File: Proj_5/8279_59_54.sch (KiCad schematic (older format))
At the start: 44 parts, among them J4 Conn_02x07_Counter_Clockwise, J5 Conn_02x07_Counter_Clockwise, SW10 Switch_SW_SPST, SW11 Switch_SW_SPST, SW12 Switch_SW_SPST, SW13 Switch_SW_SPST, SW14 Switch_SW_SPST, SW15 Switch_SW_SPST, SW16 Switch_SW_SPST, SW17 Switch_SW_SPST, SW18 Switch_SW_SPST, SW19 Switch_SW_SPST, SW2 Shift, SW20 Switch_SW_SPST, SW21 Switch_SW_SPST, SW22 Switch_SW_SPST, SW23 Switch_SW_SPST, SW24 NMI Button, SW25 Reset Button, SW26 IR0 Button, SW3 Switch_SW_SPST, SW4 Switch_SW_SPST, SW5 Switch_SW_SPST, SW6 Switch_SW_SPST, SW7 CTRL, SW8 Switch_SW_SPST, SW9 Switch_SW_SPST, U10 8259, U11 8254, U17 pkd8279, U18 74LS138, U48 MAX6816, U49 MAX6816, U50 MAX6816

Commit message: Destroyed errors
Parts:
- removed U?: 74LVC1G11, symbol 74xGxx:74LVC1G11
- removed U?: 74LVC1G08, symbol 74xGxx:74LVC1G08
- added U35, U58: 74AHC1G02, symbol 74xGxx:74AHC1G02
- added U38: 74LVC1G08, symbol 74xGxx:74LVC1G08
- gave numbers to parts that had none: 1
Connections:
- net A16: now also U35.2
- net A17: now also U35.1
- net A18: now also U58.2
- net A19: now also U58.1
- net GND: now also U35.3 (GND), U38.3 (GND), U58.3 (GND)
- net VCC: now also U35.5 (VCC), U38.5 (VCC), U58.5 (VCC)
- net at U60.1 (I1): now also U38.4
- new net: U38.1, U58.4
- new net: U35.4, U38.2
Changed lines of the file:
@@
 	7200 2700 7350 2700
 $Comp
-L Logic_Programmable:PAL16L8 U?
+L Logic_Programmable:PAL16L8 U60
 U 1 1 5ED93710
 P 2300 2350
-F 0 "U?" H 2300 3231 50  0000 C CNN
+F 0 "U60" H 2300 3231 50  0000 C CNN
 F 1 "PAL16L8" H 2300 3140 50  0000 C CNN
 F 2 "" H 2300 2350 50  0001 C CNN
@@
 Text HLabel 1800 2750 0    50   Input ~ 0
 A9
-$Comp
-L 74xGxx:74LVC1G11 U?
-U 1 1 5EE4156C
-P 1300 1850
-F 0 "U?" H 1300 2164 50  0000 C CNN
-F 1 "74LVC1G11" H 1300 2073 50  0000 C CNN
-F 2 "" H 1300 1850 50  0001 C CNN
-F 3 "http://www.ti.com/lit/sg/scyt129e/scyt129e.pdf" H 1300 1850 50  0001 C CNN
-	1    1300 1850
-	1    0    0    -1
-$EndComp
-$Comp
-L 74xGxx:74LVC1G08 U?
-U 1 1 5EE43827
-P 1000 2200
-F 0 "U?" V 1021 2070 50  0000 R CNN
-F 1 "74LVC1G08" V 930 2070 50  0000 R CNN
-F 2 "" H 1000 2200 50  0001 C CNN
-F 3 "http://www.ti.com/lit/sg/scyt129e/scyt129e.pdf" H 1000 2200 50  0001 C CNN
-	1    1000 2200
-	0    -1   -1   0
-$EndComp
-Text HLabel 950  2500 3    50   Input ~ 0
-A19
-Text HLabel 1050 2500 3    50   Input ~ 0
-A18
-Text HLabel 1000 1850 0    50   Input ~ 0
-A17
-Text HLabel 1000 1750 0    50   Input ~ 0
-A16
-Wire Wire Line
-	1600 1850 1800 1850
 Text HLabel 2800 2150 2    50   Input ~ 0
 A4
@@
 	5550 800  6450 800
 $Comp
-L power:GND #PWR?
+L power:GND #PWR082
 U 1 1 5EF0D1C7
 P 2300 2950
-F 0 "#PWR?" H 2300 2700 50  0001 C CNN
+F 0 "#PWR082" H 2300 2700 50  0001 C CNN
 F 1 "GND" H 2305 2777 50  0000 C CNN
 F 2 "" H 2300 2950 50  0001 C CNN
@@
 $EndComp
 $Comp
-L power:GND #PWR?
+L power:GND #PWR097
 U 1 1 5EF1007D
 P 5550 5650
-F 0 "#PWR?" H 5550 5400 50  0001 C CNN
+F 0 "#PWR097" H 5550 5400 50  0001 C CNN
 F 1 "GND" H 5555 5477 50  0000 C CNN
 F 2 "" H 5550 5650 50  0001 C CNN
@@
 	1    0    0    -1
 $EndComp
+$Comp
+L 74xGxx:74AHC1G02 U58
+U 1 1 5F4DAB3E
+P 1450 1000
+F 0 "U58" V 1379 1130 50  0000 L CNN
+F 1 "74AHC1G02" V 1470 1130 50  0000 L CNN
+F 2 "" H 1450 1000 50  0001 C CNN
+F 3 "http://www.ti.com/lit/sg/scyt129e/scyt129e.pdf" H 1450 1000 50  0001 C CNN
+	1    1450 1000
+	0    1    1    0
+$EndComp
+$Comp
+L 74xGxx:74AHC1G02 U35
+U 1 1 5F4DE98E
+P 1100 1250
+F 0 "U35" H 1075 1517 50  0000 C CNN
+F 1 "74AHC1G02" H 1075 1426 50  0000 C CNN
+F 2 "" H 1100 1250 50  0001 C CNN
+F 3 "http://www.ti.com/lit/sg/scyt129e/scyt129e.pdf" H 1100 1250 50  0001 C CNN
+	1    1100 1250
+	1    0    0    -1
+$EndComp
+$Comp
+L 74xGxx:74LVC1G08 U38
+U 1 1 5F4E0E05
+P 1400 1550
+F 0 "U38" V 1329 1680 50  0000 L CNN
+F 1 "74LVC1G08" V 1420 1680 50  0000 L CNN
+F 2 "" H 1400 1550 50  0001 C CNN
+F 3 "http://www.ti.com/lit/sg/scyt129e/scyt129e.pdf" H 1400 1550 50  0001 C CNN
+	1    1400 1550
+	0    1    1    0
+$EndComp
+Wire Wire Line
+	1400 1850 1400 1800
+Wire Wire Line
+	1400 1850 1800 1850
+Text HLabel 1500 700  1    50   Input ~ 0
+A19
+Text HLabel 1400 700  1    50   Input ~ 0
+A18
+Text HLabel 800  1200 0    50   Input ~ 0
+A17
+Text HLabel 800  1300 0    50   Input ~ 0
+A16
 $EndSCHEMATC

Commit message: 11 errors left
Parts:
- removed U35, U58: 74AHC1G02, symbol 74xGxx:74AHC1G02
- removed U38: 74LVC1G08, symbol 74xGxx:74LVC1G08
- removed U60: PAL16L8, symbol Logic_Programmable:PAL16L8
- added U35, U38: PAL16L8, symbol Logic_Programmable:PAL16L8
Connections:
- net A0: now also U38.8 (I8)
- net A1: now also U38.7 (I7); no longer U10.27 (A0), U17.21 (A0)
- net A10: now also U35.11 (I10)
- net A11: now also U35.9 (I9)
- net A12: now also U35.8 (I8)
- net A13: now also U35.7 (I7)
- net A14: now also U35.6 (I6)
- net A15: now also U35.5 (I5)
- net A16: now also U35.4 (I4)
- net A17: now also U35.3 (I3)
- net A18: now also U35.2 (I2)
- net A19: now also U35.1 (I1)
- net A2: now also U38.6 (I6)
- net A3: now also U38.5 (I5)
- net A4: now also U38.4 (I4)
- net A5: now also U38.3 (I3)
- net A6: now also U38.2 (I2)
- net A7: now also U38.1 (I1)
- net A8: now also U35.17 (I03)
- net A9: now also U35.18 (IO2)
- net GND: now also C19.2, U35.10 (GND), U38.10 (GND)
- net VCC: now also U35.20 (VCC), U38.20 (VCC)
- net at U17.22 (~CS): now also U38.17 (I03); no longer U10.1 (~CS~)
- net at U11.19 (A0): now also U38.14 (IO6)
- net at U11.20 (A1): now also U38.13 (IO7)
- net at U11.21 (~CS~): now also U38.15 (IO5)
- net INT: now reaches U10.17 (INT)
- net ~INTA: now reaches U10.26 (~INTA~)
- new net: U17.21 (A0), U38.16 (IO4)
- new net: U10.1 (~CS~), U38.19 (IO1)
- new net: U10.27 (A0), U38.18 (IO2)
- new net: U35.19 (IO1), U38.11 (I10)
- no-connect marks 22 -> 28
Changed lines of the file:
@@
 L power:VCC #PWR062
 U 1 1 5EA94B2B
-P 5100 3150
-F 0 "#PWR062" H 5100 3000 50  0001 C CNN
-F 1 "VCC" H 5118 3323 50  0000 C CNN
-F 2 "" H 5100 3150 50  0001 C CNN
-F 3 "" H 5100 3150 50  0001 C CNN
-	1    5100 3150
+P 6000 3150
+F 0 "#PWR062" H 6000 3000 50  0001 C CNN
+F 1 "VCC" H 6018 3323 50  0000 C CNN
+F 2 "" H 6000 3150 50  0001 C CNN
+F 3 "" H 6000 3150 50  0001 C CNN
+	1    6000 3150
 	0    -1   -1   0
 $EndComp
@@
 Wire Wire Line
 	7200 2850 7200 2700
-Connection ~ 6200 3150
 Wire Wire Line
 	6950 3150 7100 3150
@@
 	5600 6150 6550 6150
 Wire Wire Line
-	5100 3150 6200 3150
-Wire Wire Line
 	5500 800  5550 800
 Wire Wire Line
@@
 Wire Wire Line
 	7200 2700 7350 2700
-$Comp
-L Logic_Programmable:PAL16L8 U60
-U 1 1 5ED93710
-P 2300 2350
-F 0 "U60" H 2300 3231 50  0000 C CNN
-F 1 "PAL16L8" H 2300 3140 50  0000 C CNN
-F 2 "" H 2300 2350 50  0001 C CNN
-F 3 "" H 2300 2350 50  0001 C CNN
-	1    2300 2350
-	1    0    0    -1
-$EndComp
-Text HLabel 1800 1950 0    50   Input ~ 0
-A15
-Text HLabel 1800 2050 0    50   Input ~ 0
-A14
-Text HLabel 1800 2150 0    50   Input ~ 0
-A13
-Text HLabel 1800 2250 0    50   Input ~ 0
-A12
-Text HLabel 1800 2350 0    50   Input ~ 0
-A11
-Text HLabel 1800 2450 0    50   Input ~ 0
-A10
-Text HLabel 2800 1950 2    50   Input ~ 0
-A6
-Text HLabel 2800 2050 2    50   Input ~ 0
-A5
-Text HLabel 1800 2550 0    50   Input ~ 0
-A7
-Text HLabel 1800 2650 0    50   Input ~ 0
-A8
-Text HLabel 1800 2750 0    50   Input ~ 0
-A9
-Text HLabel 2800 2150 2    50   Input ~ 0
-A4
-Text HLabel 2800 2250 2    50   Input ~ 0
-A3
-Text HLabel 2800 2350 2    50   Input ~ 0
-A2
-Text HLabel 2800 2450 2    50   Input ~ 0
-A0
-Wire Wire Line
-	2800 2550 5200 2550
-Wire Wire Line
-	5200 2550 5200 2300
 Wire Wire Line
 	5200 2300 5850 2300
 Wire Wire Line
-	5200 2550 5200 4850
-Wire Wire Line
-	5200 4850 5550 4850
-Connection ~ 5200 2550
-Text HLabel 5550 5150 0    50   Input ~ 0
-A1
-Text HLabel 5850 2100 0    50   Input ~ 0
-A1
-NoConn ~ 2800 1850
-Wire Wire Line
-	5550 800  5550 1650
-Wire Wire Line
-	5550 1650 2300 1650
+	5550 800  5550 1450
 Connection ~ 5550 800
 Wire Wire Line
 	5550 800  6450 800
-$Comp
-L power:GND #PWR082
-U 1 1 5EF0D1C7
-P 2300 2950
-F 0 "#PWR082" H 2300 2700 50  0001 C CNN
-F 1 "GND" H 2305 2777 50  0000 C CNN
-F 2 "" H 2300 2950 50  0001 C CNN
-F 3 "" H 2300 2950 50  0001 C CNN
-	1    2300 2950
-	1    0    0    -1
-$EndComp
 $Comp
 L power:GND #PWR097
@@
 $EndComp
 $Comp
-L 74xGxx:74AHC1G02 U58
-U 1 1 5F4DAB3E
-P 1450 1000
-F 0 "U58" V 1379 1130 50  0000 L CNN
-F 1 "74AHC1G02" V 1470 1130 50  0000 L CNN
-F 2 "" H 1450 1000 50  0001 C CNN
-F 3 "http://www.ti.com/lit/sg/scyt129e/scyt129e.pdf" H 1450 1000 50  0001 C CNN
-	1    1450 1000
-	0    1    1    0
-$EndComp
-$Comp
-L 74xGxx:74AHC1G02 U35
-U 1 1 5F4DE98E
-P 1100 1250
-F 0 "U35" H 1075 1517 50  0000 C CNN
-F 1 "74AHC1G02" H 1075 1426 50  0000 C CNN
-F 2 "" H 1100 1250 50  0001 C CNN
-F 3 "http://www.ti.com/lit/sg/scyt129e/scyt129e.pdf" H 1100 1250 50  0001 C CNN
-	1    1100 1250
-	1    0    0    -1
-$EndComp
-$Comp
-L 74xGxx:74LVC1G08 U38
-U 1 1 5F4E0E05
-P 1400 1550
-F 0 "U38" V 1329 1680 50  0000 L CNN
-F 1 "74LVC1G08" V 1420 1680 50  0000 L CNN
-F 2 "" H 1400 1550 50  0001 C CNN
-F 3 "http://www.ti.com/lit/sg/scyt129e/scyt129e.pdf" H 1400 1550 50  0001 C CNN
-	1    1400 1550
-	0    1    1    0
-$EndComp
-Wire Wire Line
-	1400 1850 1400 1800
-Wire Wire Line
-	1400 1850 1800 1850
-Text HLabel 1500 700  1    50   Input ~ 0
+L Logic_Programmable:PAL16L8 U35
+U 1 1 5EC20107
+P 1350 4050
+F 0 "U35" H 1350 4931 50  0000 C CNN
+F 1 "PAL16L8" H 1350 4840 50  0000 C CNN
+F 2 "" H 1350 4050 50  0001 C CNN
+F 3 "" H 1350 4050 50  0001 C CNN
+	1    1350 4050
+	1    0    0    -1
+$EndComp
+Text HLabel 850  3550 0    50   Input ~ 0
 A19
-Text HLabel 1400 700  1    50   Input ~ 0
+Text HLabel 850  3650 0    50   Input ~ 0
 A18
-Text HLabel 800  1200 0    50   Input ~ 0
+Text HLabel 850  3750 0    50   Input ~ 0
 A17
-Text HLabel 800  1300 0    50   Input ~ 0
+Text HLabel 850  3850 0    50   Input ~ 0
 A16
+Text HLabel 850  3950 0    50   Input ~ 0
+A15
+Text HLabel 850  4050 0    50   Input ~ 0
+A14
+Text HLabel 850  4150 0    50   Input ~ 0
+A13
+Text HLabel 850  4250 0    50   Input ~ 0
+A12
+Text HLabel 850  4350 0    50   Input ~ 0
+A11
+Text HLabel 850  4450 0    50   Input ~ 0
+A10
+Text HLabel 1850 3650 2    50   Input ~ 0
+A9
+Text HLabel 1850 3750 2    50   Input ~ 0
+A8
+$Comp
+L Logic_Programmable:PAL16L8 U38
+U 1 1 5ECCAFFC
+P 1400 2150
+F 0 "U38" H 1400 3031 50  0000 C CNN
+F 1 "PAL16L8" H 1400 2940 50  0000 C CNN
+F 2 "" H 1400 2150 50  0001 C CNN
+F 3 "" H 1400 2150 50  0001 C CNN
+	1    1400 2150
+	1    0    0    -1
+$EndComp
+Wire Wire Line
+	1850 3550 1850 3000
+Wire Wire Line
+	1850 3000 900  3000
+Wire Wire Line
+	900  3000 900  2550
+Text HLabel 900  1650 0    50   Input ~ 0
+A7
+Text HLabel 900  1750 0    50   Input ~ 0
+A6
+Text HLabel 900  1850 0    50   Input ~ 0
+A5
+Text HLabel 900  1950 0    50   Input ~ 0
+A4
+Text HLabel 900  2050 0    50   Input ~ 0
+A3
+Text HLabel 900  2150 0    50   Input ~ 0
+A2
+Text HLabel 900  2250 0    50   Input ~ 0
+A1
+Text HLabel 900  2350 0    50   Input ~ 0
+A0
+Wire Wire Line
+	1400 1450 2100 1450
+Wire Wire Line
+	1900 1650 5200 1650
+Wire Wire Line
+	5200 1650 5200 2300
+Connection ~ 6200 3150
+Wire Wire Line
+	1900 1850 5000 1850
+Wire Wire Line
+	5000 1850 5000 4850
+Wire Wire Line
+	5000 4850 5550 4850
+Wire Wire Line
+	1900 1750 5100 1750
+Wire Wire Line
+	5100 1750 5100 2100
+Wire Wire Line
+	5100 2100 5850 2100
+Wire Wire Line
+	5550 5150 4900 5150
+Wire Wire Line
+	4900 5150 4900 1950
+Wire Wire Line
+	1900 1950 4900 1950
+Wire Wire Line
+	1900 2050 4600 2050
+Wire Wire Line
+	4600 2050 4600 8200
+Wire Wire Line
+	4600 8200 5950 8200
+Wire Wire Line
+	1900 2150 4400 2150
+Wire Wire Line
+	4400 2150 4400 7900
+Wire Wire Line
+	4400 7900 5950 7900
+Wire Wire Line
+	1900 2250 4200 2250
+Wire Wire Line
+	4200 2250 4200 8000
+Wire Wire Line
+	4200 8000 5950 8000
+NoConn ~ 1900 2350
+NoConn ~ 900  2450
+NoConn ~ 1850 3850
+NoConn ~ 1850 3950
+NoConn ~ 1850 4050
+NoConn ~ 1850 4150
+NoConn ~ 1850 4250
+Wire Wire Line
+	2100 1450 2100 3350
+Wire Wire Line
+	2100 3350 1350 3350
+Connection ~ 2100 1450
+Wire Wire Line
+	2100 1450 5550 1450
+$Comp
+L power:GND #PWR027
+U 1 1 5EEA610B
+P 1400 2750
+F 0 "#PWR027" H 1400 2500 50  0001 C CNN
+F 1 "GND" H 1405 2577 50  0000 C CNN
+F 2 "" H 1400 2750 50  0001 C CNN
+F 3 "" H 1400 2750 50  0001 C CNN
+	1    1400 2750
+	1    0    0    -1
+$EndComp
+$Comp
+L power:GND #PWR025
+U 1 1 5EEA70E4
+P 1350 4650
+F 0 "#PWR025" H 1350 4400 50  0001 C CNN
+F 1 "GND" H 1355 4477 50  0000 C CNN
+F 2 "" H 1350 4650 50  0001 C CNN
+F 3 "" H 1350 4650 50  0001 C CNN
+	1    1350 4650
+	1    0    0    -1
+$EndComp
+$Comp
+L power:GND #PWR0131
+U 1 1 5EEC84CD
+P 14950 2400
+F 0 "#PWR0131" H 14950 2150 50  0001 C CNN
+F 1 "GND" H 14955 2227 50  0000 C CNN
+F 2 "" H 14950 2400 50  0001 C CNN
+F 3 "" H 14950 2400 50  0001 C CNN
+	1    14950 2400
+	1    0    0    -1
+$EndComp
+Text HLabel 5850 2800 0    50   Input ~ 0
+~INTA
+Text HLabel 5850 2700 0    50   Output ~ 0
+INT
+Wire Wire Line
+	6200 3150 6000 3150
 $EndSCHEMATC

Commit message: Added 5 Footprints
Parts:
- U17: footprint pkd8279 -> parts:pkd8279
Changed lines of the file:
@@
 F 0 "U17" H 6575 4137 60  0000 C CNN
 F 1 "pkd8279" H 6575 4031 60  0000 C CNN
-F 2 "pkd8279" H 6550 4140 60  0001 C CNN
+F 2 "parts:pkd8279" H 6550 4140 60  0001 C CNN
 F 3 "" H 5550 3750 60  0000 C CNN
 	1    5550 3750

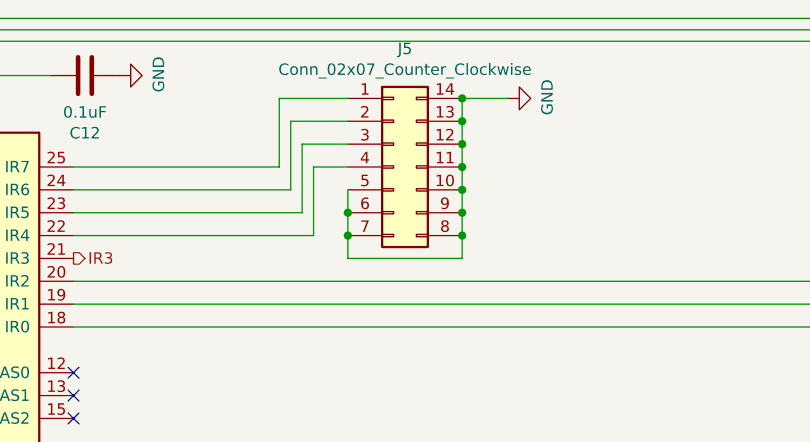
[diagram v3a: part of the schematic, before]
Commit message: Added at least 4 Footprints
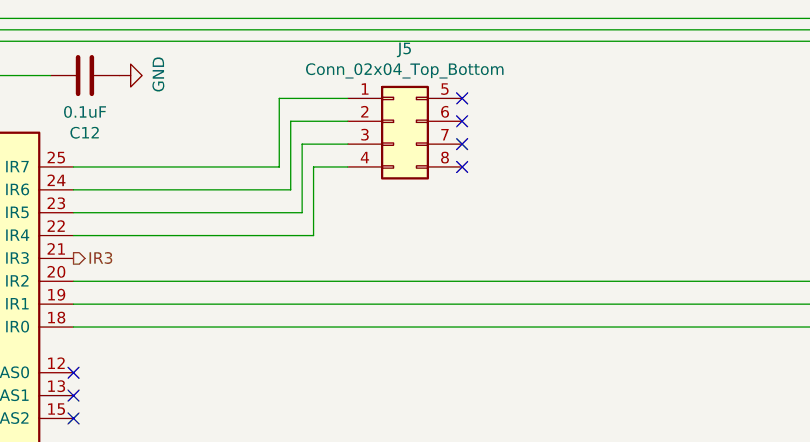
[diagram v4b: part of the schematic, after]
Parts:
- removed J5: Conn_02x07_Counter_Clockwise, symbol Connector_Generic:Conn_02x07_Counter_Clockwise
- added J5: Conn_02x04_Top_Bottom, Connector_PinHeader_1.00mm:PinHeader_2x04_P1.00mm_Vertical, symbol Connector_Generic:Conn_02x04_Top_Bottom
- C11, C12, C13, C15, C18, C19: footprint (none) -> Capacitor_Tantalum_SMD:CP_EIA-1608-08_AVX-J
- J4: footprint (none) -> Connector_PinHeader_1.00mm:PinHeader_2x07_P1.00mm_Vertical
- R17: footprint (none) -> Resistor_SMD:R_0201_0603Metric
- SW10, SW11, SW12, SW13, SW14, SW15, SW16, SW17, SW18, SW19, SW2, SW20, SW21, SW22, SW23, SW24, SW25, SW26, SW3, SW4, SW5, SW6, SW7, SW8, SW9: footprint (none) -> Button_Switch_SMD:SW_SPST_B3U-1000P-B
- U18: footprint (none) -> Package_DIP:DIP-16_W7.62mm
- U35, U38: footprint (none) -> Package_DIP:DIP-20_W7.62mm
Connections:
- net at U10.22 (IR4): now also J5.4 (Pin_4)
- net at U10.23 (IR5): now also J5.3 (Pin_3)
- net at U10.24 (IR6): now also J5.2 (Pin_2)
- net at U10.25 (IR7): now also J5.1 (Pin_1)
- no-connect marks 28 -> 32

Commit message: Playing with PCB placements
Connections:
- net GND: no longer J4.10 (Pin_10), J4.11 (Pin_11), J4.12 (Pin_12), J4.13 (Pin_13), J4.14 (Pin_14), J4.9 (Pin_9)
- no-connect marks 32 -> 38
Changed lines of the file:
@@
 Wire Wire Line
 	8400 8000 8400 7500
-Wire Wire Line
-	8400 7400 8400 7300
-Connection ~ 8400 7000
-Wire Wire Line
-	8400 7000 8400 6900
-Connection ~ 8400 7100
-Wire Wire Line
-	8400 7100 8400 7000
-Connection ~ 8400 7200
-Wire Wire Line
-	8400 7200 8400 7100
-Connection ~ 8400 7300
-Wire Wire Line
-	8400 7300 8400 7200
-Wire Wire Line
-	8400 6900 8550 6900
-Connection ~ 8400 6900
-$Comp
-L power:GND #PWR070
-U 1 1 5F6F628E
-P 8550 6900
-F 0 "#PWR070" H 8550 6650 50  0001 C CNN
-F 1 "GND" H 8555 6727 50  0000 C CNN
-F 2 "" H 8550 6900 50  0001 C CNN
-F 3 "" H 8550 6900 50  0001 C CNN
-	1    8550 6900
-	0    -1   -1   0
-$EndComp
 NoConn ~ 7600 3800
 NoConn ~ 7050 2100
@@
 NoConn ~ 8750 1100
 NoConn ~ 8750 1200
+NoConn ~ 8400 6900
+NoConn ~ 8400 7000
+NoConn ~ 8400 7100
+NoConn ~ 8400 7200
+NoConn ~ 8400 7300
+NoConn ~ 8400 7400
 $EndSCHEMATC

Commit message: Hey Collin
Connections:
- net at U10.22 (IR4): now also J5.1 (Pin_1); no longer J5.4 (Pin_4)
- net at U10.24 (IR6): now also J5.5 (Pin_5); no longer J5.2 (Pin_2)
- net at U10.25 (IR7): now also J5.7 (Pin_7); no longer J5.1 (Pin_1)
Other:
- moved on the sheet: J5
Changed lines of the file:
@@
 	7050 1200 7950 1200
 Wire Wire Line
-	7950 1200 7950 900
-Wire Wire Line
-	7950 900  8250 900
-Wire Wire Line
 	7050 1300 8000 1300
-Wire Wire Line
-	8000 1300 8000 1000
-Wire Wire Line
-	8000 1000 8250 1000
-Wire Wire Line
-	7050 1400 8050 1400
-Wire Wire Line
-	8050 1400 8050 1100
-Wire Wire Line
-	8050 1100 8250 1100
-Wire Wire Line
-	7050 1500 8100 1500
-Wire Wire Line
-	8100 1500 8100 1200
-Wire Wire Line
-	8100 1200 8250 1200
 Wire Wire Line
 	4500 650  10800 650
@@
 	5600 6150 6550 6150
 Wire Wire Line
-	5500 800  5550 800
-Wire Wire Line
 	9850 6450 9850 6650
 Wire Wire Line
@@
 Wire Wire Line
 	5200 2300 5850 2300
-Wire Wire Line
-	5550 800  5550 1450
-Connection ~ 5550 800
-Wire Wire Line
-	5550 800  6450 800
 $Comp
 L power:GND #PWR097
@@
 A0
 Wire Wire Line
-	1400 1450 2100 1450
+	1400 1450 1850 1450
 Wire Wire Line
 	1900 1650 5200 1650
@@
 Wire Wire Line
 	2100 3350 1350 3350
-Connection ~ 2100 1450
-Wire Wire Line
-	2100 1450 5550 1450
 $Comp
 L power:GND #PWR027
@@
 L Connector_Generic:Conn_02x04_Top_Bottom J5
 U 1 1 5EBE66D2
-P 8450 1000
-F 0 "J5" H 8500 1317 50  0000 C CNN
-F 1 "Conn_02x04_Top_Bottom" H 8500 1226 50  0000 C CNN
-F 2 "Connector_PinHeader_1.00mm:PinHeader_2x04_P1.00mm_Vertical" H 8450 1000 50  0001 C CNN
-F 3 "~" H 8450 1000 50  0001 C CNN
-	1    8450 1000
-	1    0    0    -1
-$EndComp
-NoConn ~ 8750 900
-NoConn ~ 8750 1000
-NoConn ~ 8750 1100
-NoConn ~ 8750 1200
+P 8550 1000
+F 0 "J5" H 8600 1317 50  0000 C CNN
+F 1 "Conn_02x04_Top_Bottom" H 8600 1226 50  0000 C CNN
+F 2 "Connector_PinHeader_1.00mm:PinHeader_2x04_P1.00mm_Vertical" H 8550 1000 50  0001 C CNN
+F 3 "~" H 8550 1000 50  0001 C CNN
+	1    8550 1000
+	-1   0    0    1
+$EndComp
 NoConn ~ 8400 6900
 NoConn ~ 8400 7000
@@
 NoConn ~ 8400 7300
 NoConn ~ 8400 7400
+Wire Wire Line
+	7050 1400 8900 1400
+Wire Wire Line
+	7050 1500 8950 1500
+Wire Wire Line
+	8950 1500 8950 1100
+NoConn ~ 8750 1000
+Wire Wire Line
+	8900 900  8750 900
+Wire Wire Line
+	8900 900  8900 1400
+Wire Wire Line
+	8750 1100 8950 1100
+NoConn ~ 8750 800
+NoConn ~ 8250 800
+NoConn ~ 8250 1000
+Wire Wire Line
+	7950 900  7950 1200
+Wire Wire Line
+	7950 900  8250 900
+Wire Wire Line
+	8000 1300 8000 1100
+Wire Wire Line
+	8000 1100 8250 1100
+$Comp
+L power:VCC #PWR?
+U 1 1 5EDA1350
+P 1850 1450
+F 0 "#PWR?" H 1850 1300 50  0001 C CNN
+F 1 "VCC" H 1868 1623 50  0000 C CNN
+F 2 "" H 1850 1450 50  0001 C CNN
+F 3 "" H 1850 1450 50  0001 C CNN
+	1    1850 1450
+	1    0    0    -1
+$EndComp
+Wire Wire Line
+	5500 800  6450 800
+Wire Wire Line
+	1850 1450 2100 1450
+Connection ~ 1850 1450
 $EndSCHEMATC

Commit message: Fixed 'Pad too close to Pad' Errors
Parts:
- J4: footprint Connector_PinHeader_1.00mm:PinHeader_2x07_P1.00mm_Vertical -> Connector_PinHeader_2.54mm:PinHeader_2x07_P2.54mm_Horizontal
- J5: footprint Connector_PinHeader_1.00mm:PinHeader_2x04_P1.00mm_Vertical -> Connector_PinHeader_2.54mm:PinHeader_2x04_P2.54mm_Horizontal
- R17: footprint Resistor_SMD:R_0201_0603Metric -> Resistor_SMD:R_1206_3216Metric
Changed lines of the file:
@@
 $Descr A2 23386 16535
 encoding utf-8
-Sheet 6 10
+Sheet 5 10
 Title ""
 Date ""
@@
 F 0 "R17" H 10620 8046 50  0000 L CNN
 F 1 "1kOhm" H 10620 7955 50  0000 L CNN
-F 2 "Resistor_SMD:R_0201_0603Metric" V 10480 8000 50  0001 C CNN
+F 2 "Resistor_SMD:R_1206_3216Metric" V 10480 8000 50  0001 C CNN
 F 3 "~" H 10550 8000 50  0001 C CNN
 	1    10550 8000
@@
 F 0 "J4" H 8150 7717 50  0000 C CNN
 F 1 "Conn_02x07_Counter_Clockwise" H 8150 7626 50  0000 C CNN
-F 2 "Connector_PinHeader_1.00mm:PinHeader_2x07_P1.00mm_Vertical" H 8100 7200 50  0001 C CNN
+F 2 "Connector_PinHeader_2.54mm:PinHeader_2x07_P2.54mm_Horizontal" H 8100 7200 50  0001 C CNN
 F 3 "~" H 8100 7200 50  0001 C CNN
 	1    8100 7200
@@
 F 0 "J5" H 8600 1317 50  0000 C CNN
 F 1 "Conn_02x04_Top_Bottom" H 8600 1226 50  0000 C CNN
-F 2 "Connector_PinHeader_1.00mm:PinHeader_2x04_P1.00mm_Vertical" H 8550 1000 50  0001 C CNN
+F 2 "Connector_PinHeader_2.54mm:PinHeader_2x04_P2.54mm_Horizontal" H 8550 1000 50  0001 C CNN
 F 3 "~" H 8550 1000 50  0001 C CNN
 	1    8550 1000
